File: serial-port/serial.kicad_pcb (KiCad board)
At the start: 2 copper layers, 49.5 x 45.7 mm, 24 parts, among them J1 12V Pwr, J2 Serial 5V, J3 XL-320, J4 AX-12A, U1 AP1117-50, U2 LM317, U3 74LS126

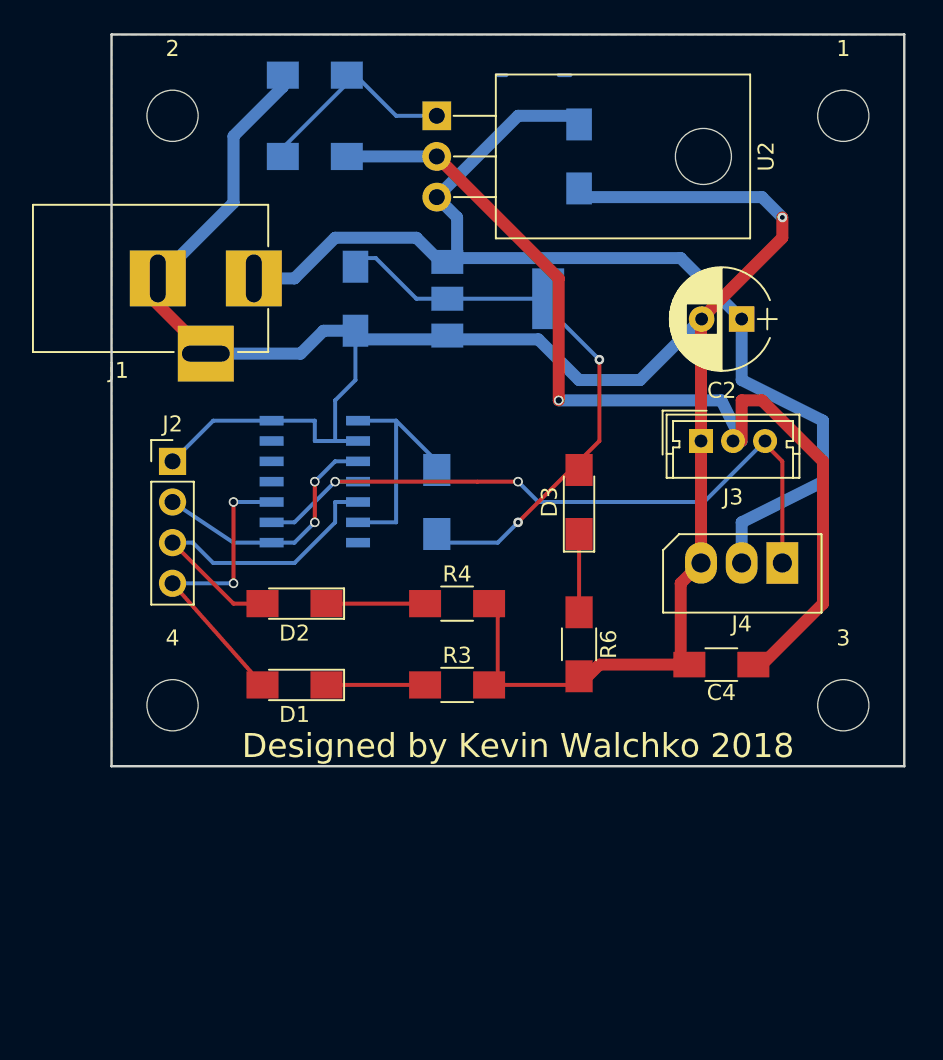
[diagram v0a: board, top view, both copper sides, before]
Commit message: serial port fixes
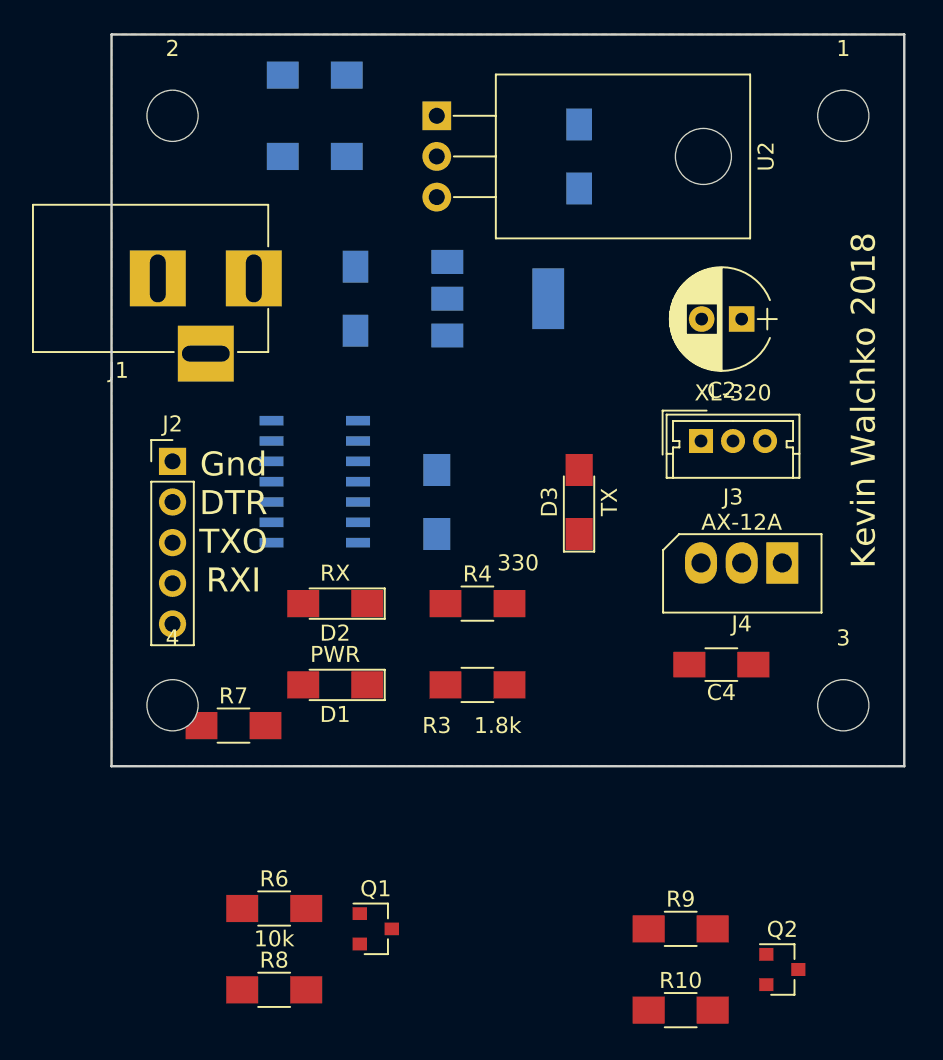
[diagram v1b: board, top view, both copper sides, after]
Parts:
- added Q1: BSS138, TO_SOT_Packages_SMD:SOT-23, F.Cu at (67.3, 69.8)
- added Q2: BSS138, TO_SOT_Packages_SMD:SOT-23, F.Cu at (92.7, 72.4)
- added R10: 10k, Resistors_SMD:R_1206_HandSoldering, F.Cu at (86.4, 74.9)
- added R7: 10k, Resistors_SMD:R_1206_HandSoldering, F.Cu at (58.4, 57.1)
- added R8: 10k, Resistors_SMD:R_1206_HandSoldering, F.Cu at (61.0, 73.7)
- added R9: 10k, Resistors_SMD:R_1206_HandSoldering, F.Cu at (86.4, 69.8)
- D1: value RX -> PWR
- D2: value TX -> RX
- D3: value PWR -> TX
- J2: value Serial 5V -> Serial; footprint Pin_Headers:Pin_Header_Straight_1x04_Pitch2.54mm -> Pin_Headers:Pin_Header_Straight_1x05_Pitch2.54mm
- R2: value 1.8k -> 330
- R3: value 330 -> 1.8k
- R5: value 10k -> 330
- R6: value 330 -> 10k
- moved R6 25.2 mm to (61.0, 68.6), turned to 0 degrees
- moved D1 2.54 mm to (64.8, 54.6)
- moved D2 2.54 mm to (64.8, 49.5)
- moved R3 1.27 mm to (73.7, 54.6)
- moved R4 1.27 mm to (73.7, 49.5)
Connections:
- D1 pad 2: RXI -> +5V
- D2 pad 2: TXO -> RXI
- D3 pad 2: +5V -> TXO
- J2 pad 2: DTR -> +3V3
- J2 pad 3: TXO -> TXO3v3
- J2 pad 4: RXI -> RXI3v3
- R1 pad 1: +8V -> Net-(D1-Pad1)
- R1 pad 2: Net-(R1-Pad2) -> GND
- R2 pad 1: Net-(R1-Pad2) -> +8V
- R2 pad 2: GND -> Net-(R2-Pad2)
- R3 pad 1: Net-(D1-Pad1) -> Net-(R2-Pad2)
- R5 pad 1: +5V -> Net-(D3-Pad1)
- R5 pad 2: Net-(R5-Pad2) -> GND
- R6 pad 1: Net-(D3-Pad1) -> +3V3
- R6 pad 2: GND -> RXI3v3
- U2 pad 1: Net-(R1-Pad2) -> Net-(R2-Pad2)
- U3 pad 1: DTR -> Net-(U3-Pad1)
- U3 pad 13: Net-(R5-Pad2) -> Net-(R7-Pad2)
- U3 pad 14: VCC -> +5V
- U3 pad 2: DATA -> Net-(U3-Pad2)
- U3 pad 3: RXI -> Net-(U3-Pad3)
- U3 pad 4: Net-(U3-Pad4) -> DTR
- U3 pad 5: Net-(U3-Pad5) -> DATA
- U3 pad 6: Net-(U3-Pad6) -> RXI
- U3 pad 8: Net-(R5-Pad2) -> Net-(R7-Pad2)
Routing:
- net GND: track 148.9 -> 0.00 mm, vias 1 -> 0
- net +12V: track 73.0 -> 0.00 mm
- net +8V: track 62.1 -> 0.00 mm, vias 1 -> 0
- net DATA: track 43.8 -> 0.00 mm, vias 2 -> 0
- net +5V: track 39.1 -> 0.00 mm, vias 2 -> 0
- net TXO: track 22.2 -> 0.00 mm
- net RXI: track 20.3 -> 0.00 mm, vias 2 -> 0
- net DTR: track 16.1 -> 0.00 mm, vias 2 -> 0
- net Net-(R5-Pad2): track 15.4 -> 0.00 mm
- net Net-(R1-Pad2): track 14.9 -> 0.00 mm
- net Net-(D2-Pad1): track 6.16 -> 0.00 mm
- net Net-(D1-Pad1): track 6.16 -> 0.00 mm
- net Net-(D3-Pad1): track 4.89 -> 0.00 mm
- net (no net): track 1.27 -> 0.00 mm
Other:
- board text added: "Gnd DTR TXO RXI"
- board text added: "Kevin Walchko 2018"
- board text removed: "Designed by Kevin Walchko 2018"

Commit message: update
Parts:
- removed 1, 2, 3, 4: , Mounting_Holes:MountingHole_3.2mm_M3
- added ?: , Mounting_Holes:MountingHole_2.2mm_M2, F.Cu at (97.8, 16.5)
- added ?: , Mounting_Holes:MountingHole_2.2mm_M2, F.Cu at (53.3, 57.1)
- added ?: , Mounting_Holes:MountingHole_2.2mm_M2, F.Cu at (97.8, 57.1)
- added ?: OSHW-Logo_7.5x8mm_SilkScreen, Symbols:OSHW-Logo_7.5x8mm_SilkScreen, F.Cu at (79.4, 38.1)
- added ?: , Mounting_Holes:MountingHole_2.2mm_M2, F.Cu at (53.3, 16.5)
- C4, R10, R3, R4, R6, R7, R8, R9: moved to B.Cu
- Q1, Q2: value BSS138 -> BS170; footprint TO_SOT_Packages_SMD:SOT-23 -> TO_SOT_Packages_THT:TO-92_Inline_Wide
- R1: moved to F.Cu
- moved R8 37.0 mm to (71.1, 38.1), turned to 180 degrees
- moved R9 36.4 mm to (59.7, 45.1), turned to 270 degrees
- moved R10 34.1 mm to (69.8, 45.1), turned to 270 degrees
- moved C4 32.5 mm to (86.4, 21.0), turned to 270 degrees
- moved R3 30.5 mm to (80.0, 24.8)
- moved Q2 28.8 mm to (71.1, 53.3), turned to 180 degrees
- moved C2 26.7 mm to (66.7, 19.1), turned to 90 degrees
- moved R6 23.8 mm to (64.8, 45.1), turned to 270 degrees
- moved D1 23.6 mm to (67.3, 31.1), turned to 0 degrees
- moved D2 22.9 mm to (87.6, 51.4), turned to 0 degrees
- moved R7 20.4 mm to (74.9, 45.1), turned to 270 degrees
- moved R5 20.4 mm to (87.6, 55.2), turned to 0 degrees
- moved U3 19.1 mm to (82.5, 43.2), turned to 180 degrees
- moved C3 18.8 mm to (84.5, 34.3)
- moved Q1 16.9 mm to (63.5, 53.3), turned to 180 degrees
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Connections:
- Q1 pad 1: RXI3v3 -> RXI
- Q1 pad 3: RXI -> RXI3v3
- Q2 pad 1: TXO3v3 -> TXO
- Q2 pad 3: TXO -> TXO3v3
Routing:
- net +12V: track 0.00 -> 58.7 mm, vias 0 -> 1
- net +8V: track 0.00 -> 58.4 mm, vias 0 -> 2
- net RXI: track 0.00 -> 49.6 mm, vias 0 -> 4
- net +5V: track 0.00 -> 43.8 mm, vias 0 -> 1
- net DTR: track 0.00 -> 43.0 mm, vias 0 -> 4
- net TXO: track 0.00 -> 36.8 mm, vias 0 -> 2
- net DATA: track 0.00 -> 30.9 mm
- net RXI3v3: track 0.00 -> 24.3 mm, vias 0 -> 2
- net GND: track 0.00 -> 22.4 mm, vias 0 -> 2
- net TXO3v3: track 0.00 -> 22.3 mm
- net Net-(R7-Pad2): track 0.00 -> 16.0 mm
- net +3V3: track 0.00 -> 11.4 mm
- net Net-(R2-Pad2): track 0.00 -> 11.0 mm
- net Net-(D2-Pad1): track 0.00 -> 9.39 mm, vias 0 -> 1
- net Net-(D3-Pad1): track 0.00 -> 6.58 mm, vias 0 -> 1
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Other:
- net class High: trace_width 0.75 -> 1.75
- board text added: "GND 3V3 TXO RXI DTR"
- board text removed: "Gnd DTR TXO RXI"
